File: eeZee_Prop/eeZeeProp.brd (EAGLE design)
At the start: 47.2 x 24.4 mm, 33 parts, among them Q1 5MHz, Q2 2N3904SMD, SW1 RESET, U1 P8X32A-Q44, U2 24LC256-I/ST, U3 NCP1117 3V3

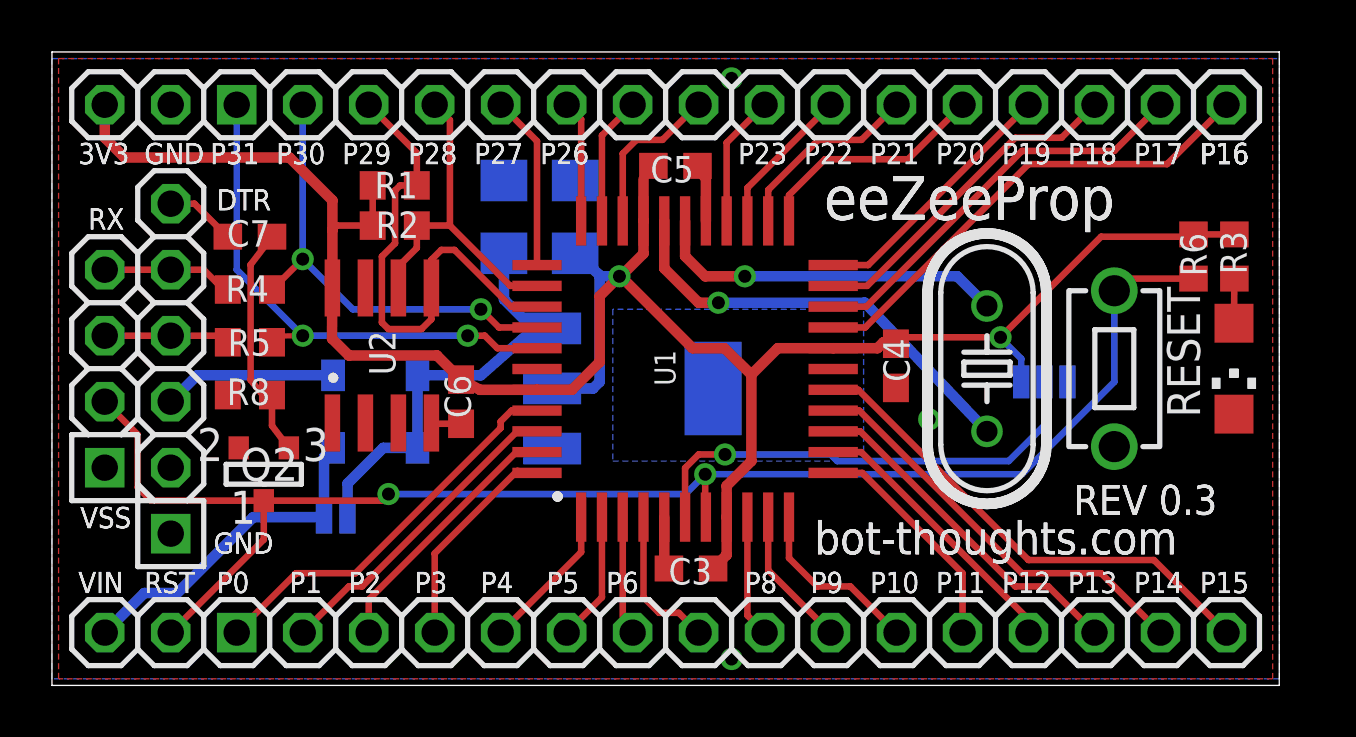
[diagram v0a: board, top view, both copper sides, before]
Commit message: Enlarged pads for SOT-23 and SOD123F for easier hand assembly. Slight tweaks to traces.
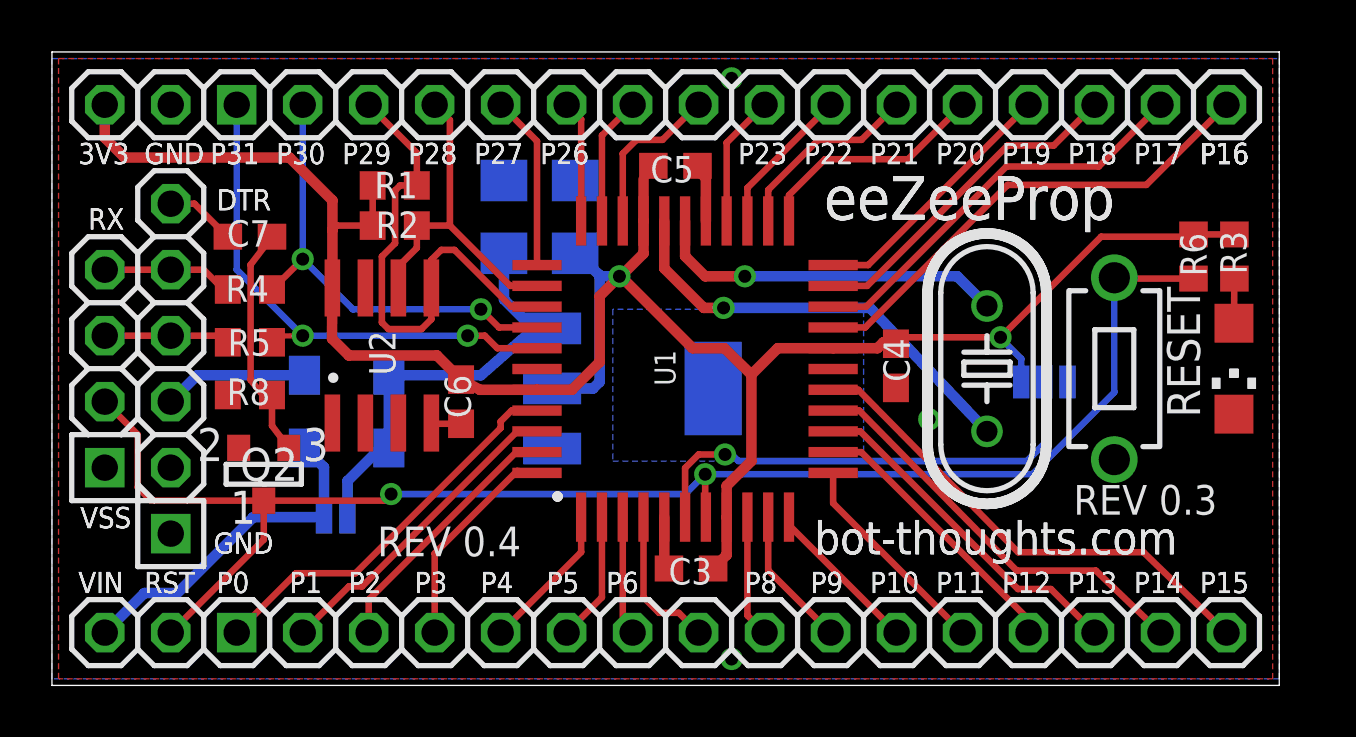
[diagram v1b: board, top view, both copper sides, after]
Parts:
- moved D1 1.10 mm to (11.3, 11.9)
- moved D2 1.10 mm to (11.3, 9.14)
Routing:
- net VUSB: track 6.67 -> 5.57 mm
- net V+: track 16.6 -> 17.4 mm
- net N$13: track 6.91 -> 6.16 mm
- net N$14: track 8.87 -> 8.21 mm
- net !RES: track 58.5 -> 59.1 mm
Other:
- board text added: "NOTE: Reconsider Regulator, 10uF caps"
- board text added: "REV 0.4"

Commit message: Minor layout tweaks
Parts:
- moved D1 1.10 mm to (12.4, 11.9)
- moved D2 1.10 mm to (12.4, 9.14)
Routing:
- net !RES: track 59.1 -> 67.2 mm
- net !BOE: track 18.7 -> 25.9 mm
- net XO: track 16.9 -> 18.2 mm
- net VUSB: track 5.57 -> 6.67 mm
- net V+: track 17.4 -> 16.7 mm
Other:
- board text added: "NOTE: Reconsider Regulator, 10uF caps Newark: C3216X5R1C106M 16V 10uF"
- board text removed: "NOTE: Reconsider Regulator, 10uF caps"

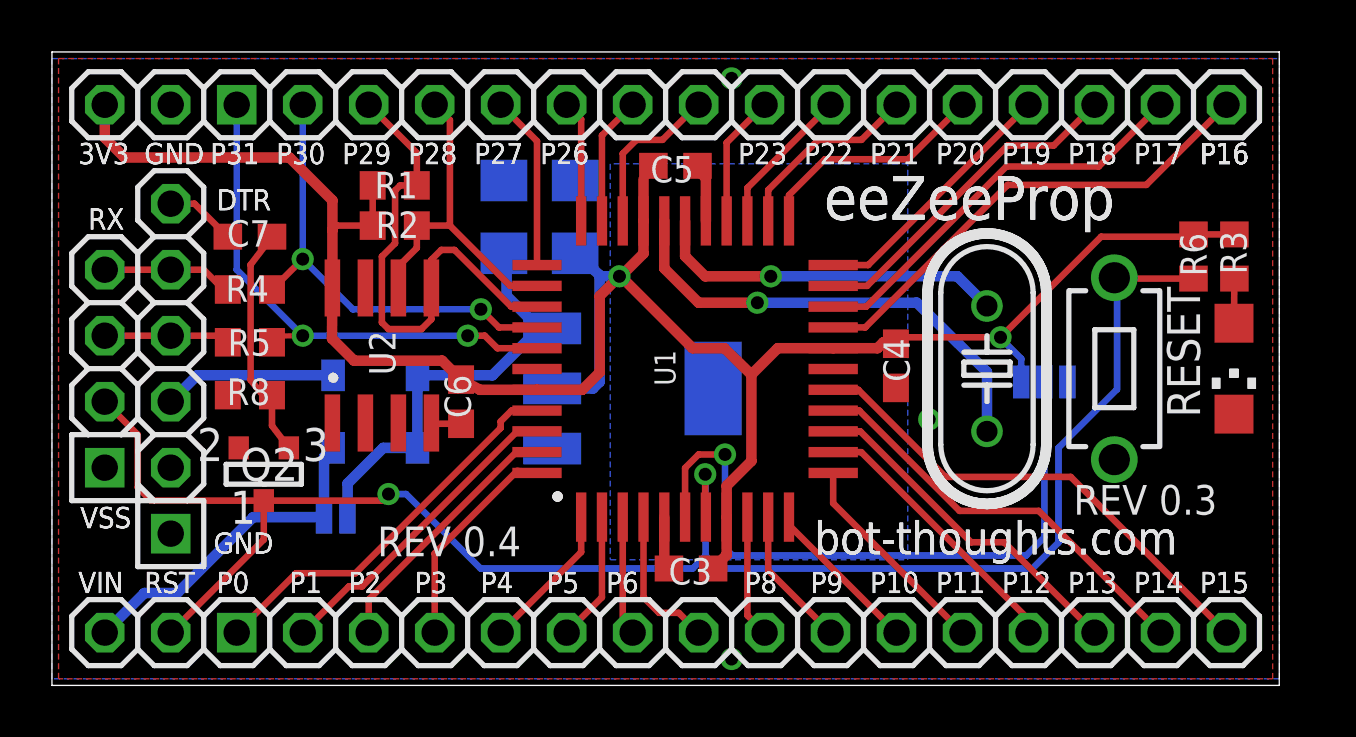
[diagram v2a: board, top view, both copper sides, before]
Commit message: Version 0.4, changes some footprints for easier rework, some mods to routing, mitered corners, some other stuff I'm forgetting.
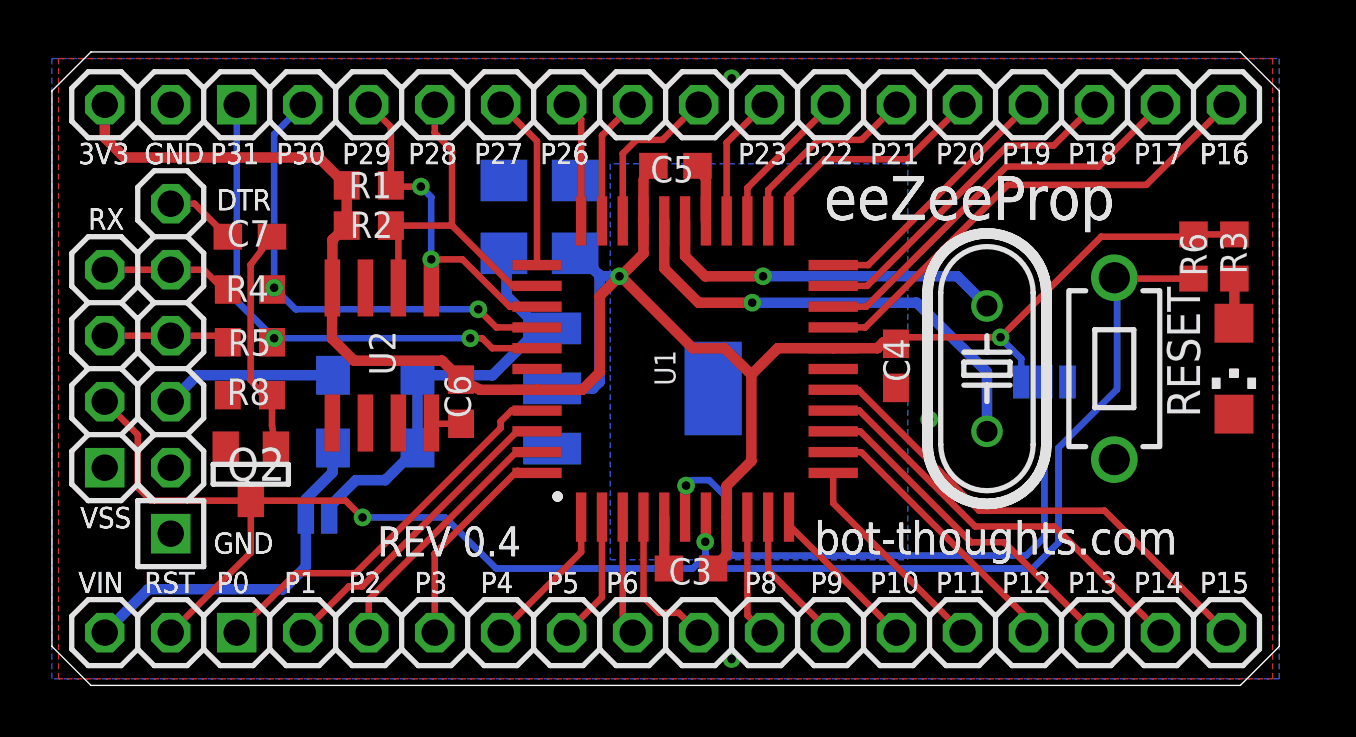
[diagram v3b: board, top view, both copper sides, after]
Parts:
- R4, R5: value 1k -> 10k
- moved R1 1.00 mm to (12.2, 19.2)
- moved R2 1.00 mm to (12.2, 17.7)
- moved SJ1 0.70 mm to (10.2, 6.48)
- moved Q2 0.50 mm to (7.63, 8.13)
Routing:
- net P29: track 19.7 -> 13.5 mm, vias 0 -> 2
- net !RES: track 67.2 -> 63.5 mm
- net !BOE: track 25.9 -> 23.8 mm
- net VDD: track 85.5 -> 83.5 mm
- net P28: track 13.2 -> 14.0 mm
- net VIN: track 13.1 -> 13.8 mm
- net P30: track 17.7 -> 18.3 mm
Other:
- outline, holes or cut-outs redrawn
- board text added: "U3"
- board text removed: "NOTE: Reconsider Regulator, 10uF caps Newark: C3216X5R1C106M 16V 10uF"
- board text removed: "REV 0.3"
